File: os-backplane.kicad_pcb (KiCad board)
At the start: 4 copper layers, 195 x 95 mm, 160 parts, among them J10 FAN, J8 PWR, J9 FPANEL, Q1 AOD4189, Q10 MMBT3904, Q11 IRFML8244, Q2 AOD4189, Q3 BSS138, Q4 BSS138, Q5 CSD18504Q5A, Q6 CSD18504Q5A, Q7 CSD18503Q5A, Q8 MMBT3904, Q9 MMBT3906, U6 LM25116MHX, U7 LM25088-1MH

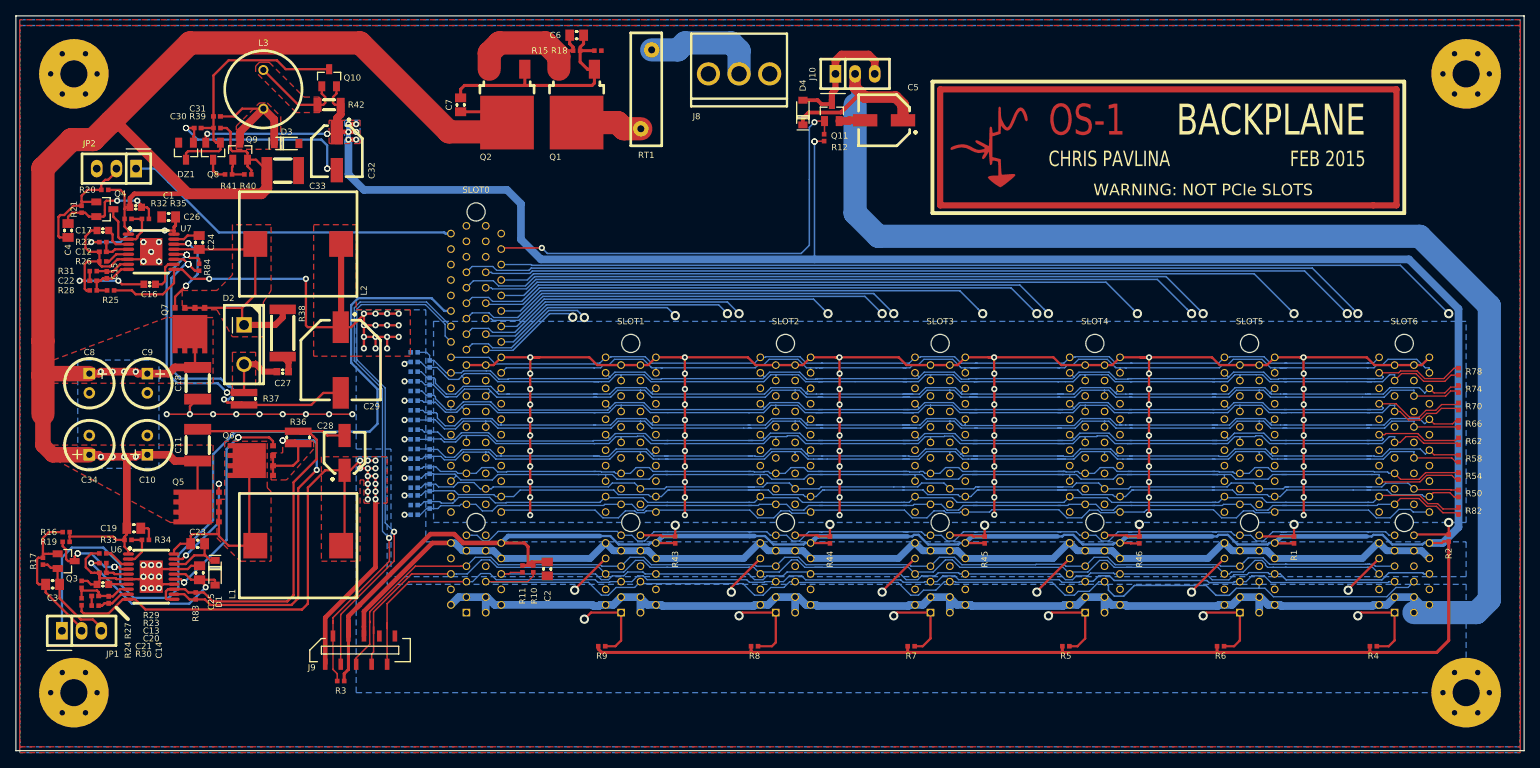
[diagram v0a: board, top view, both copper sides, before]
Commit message: Reannotated parts
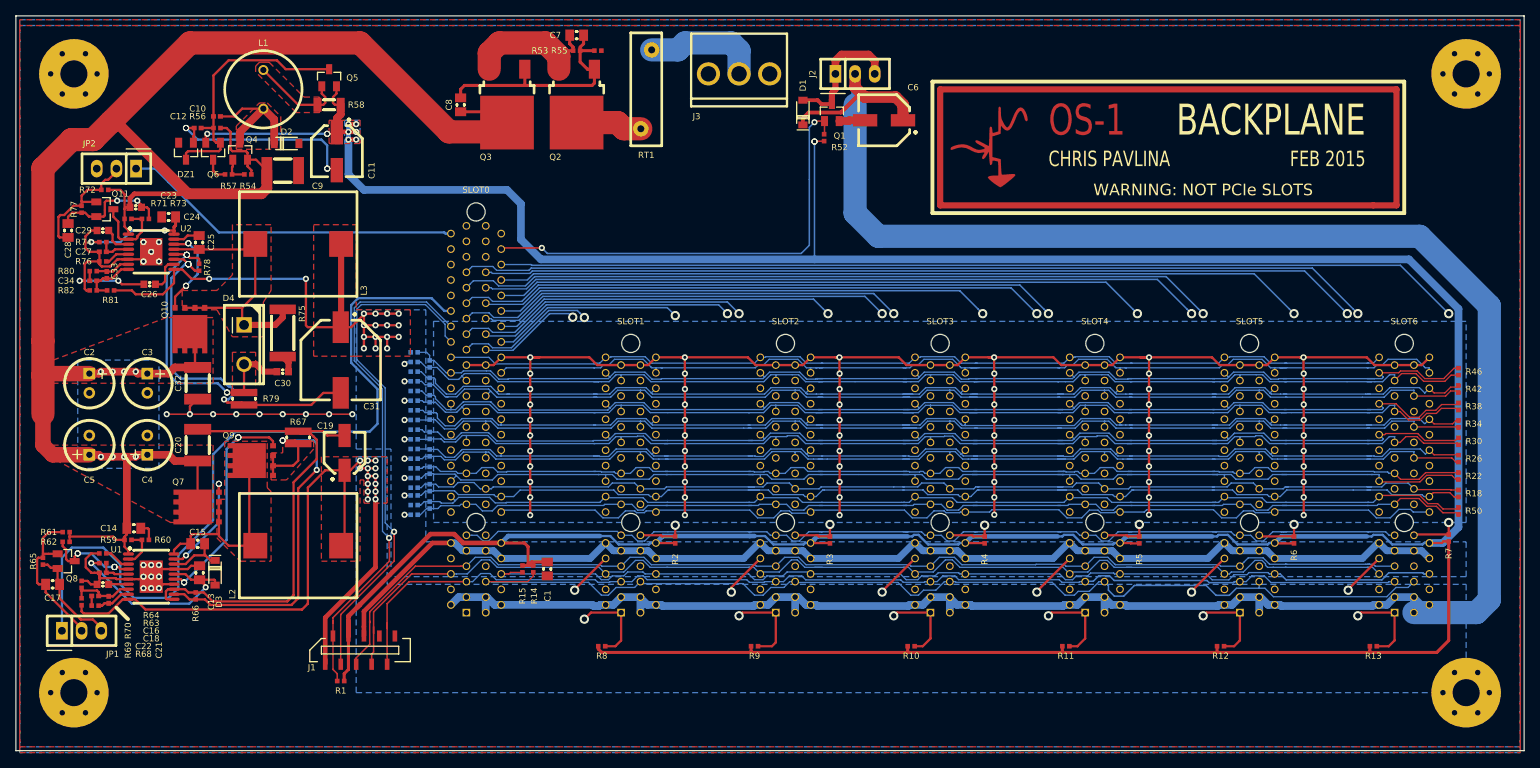
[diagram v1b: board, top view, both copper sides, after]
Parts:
- renumbered C2 to C1, C31 to C10, C32 to C11, C30 to C12, C25 to C13, C19 to C14, C23 to C15, C13 to C16, C3 to C17, C20 to C18, C28 to C19, C8 to C2, C11 to C20, C14 to C21, C21 to C22, C1 to C23, C26 to C24, C24 to C25, C16 to C26, C12 to C27, C4 to C28, C17 to C29, C9 to C3, C27 to C30, C29 to C31, C18 to C32, C15 to C33, C22 to C34, C10 to C4, C34 to C5, C5 to C6, C6 to C7, C7 to C8, C33 to C9, D4 to D1, D3 to D2, D1 to D3, D2 to D4, J9 to J1, J10 to J2, J8 to J3, L3 to L1, L1 to L2, L2 to L3, Q11 to Q1, Q7 to Q10, Q4 to Q11, Q1 to Q2, Q2 to Q3, Q9 to Q4, Q10 to Q5, Q8 to Q6, Q5 to Q7, Q3 to Q8, Q6 to Q9, R3 to R1, R7 to R10, R5 to R11, R6 to R12, R4 to R13, R10 to R14, R11 to R15, R47 to R16, R48 to R17, R50 to R18, R49 to R19, R43 to R2, R51 to R20, R52 to R21, R54 to R22, R53 to R23, R55 to R24, R56 to R25, R58 to R26, R57 to R27, R59 to R28, R60 to R29, R44 to R3, R62 to R30, R61 to R31, R63 to R32, R64 to R33, R66 to R34, R65 to R35, R67 to R36, R68 to R37, R70 to R38, R69 to R39, R45 to R4, R71 to R40, R72 to R41, R74 to R42, R73 to R43, R75 to R44, R76 to R45, R78 to R46, R77 to R47, R79 to R48, R80 to R49, R46 to R5, R82 to R50, R81 to R51, R12 to R52, R15 to R53, R40 to R54, R18 to R55, R39 to R56, R41 to R57, R42 to R58, R33 to R59, R1 to R6, R34 to R60, R16 to R61, R19 to R62, R23 to R63, R29 to R64, R17 to R65, R83 to R66, R36 to R67, R30 to R68, R24 to R69, R2 to R7, R27 to R70, R32 to R71, R20 to R72, R35 to R73, R22 to R74, R38 to R75, R26 to R76, R21 to R77, R84 to R78, R37 to R79, R9 to R8, R31 to R80, R25 to R81, R28 to R82, R8 to R9, U6 to U1, U7 to U2, W2 to W1, W1 to W2, W4 to W3, W3 to W4
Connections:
- R1 pad 2: Net-(R3-Pad2) -> +3.3SB
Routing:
- net +3.3SB: track 553.2 -> 554.1 mm
- net Net-(R3-Pad2): track 0.95 -> 0.00 mm
- added copper zone on F.Cu, net /Power/Supply3V3/CS+
- added copper zone on F.Cu, net /Power/Supply3V3/SW
- removed copper zone on F.Cu, net /Power/3CS
- removed copper zone on F.Cu, net /Power/3SW

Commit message: Added extra supports
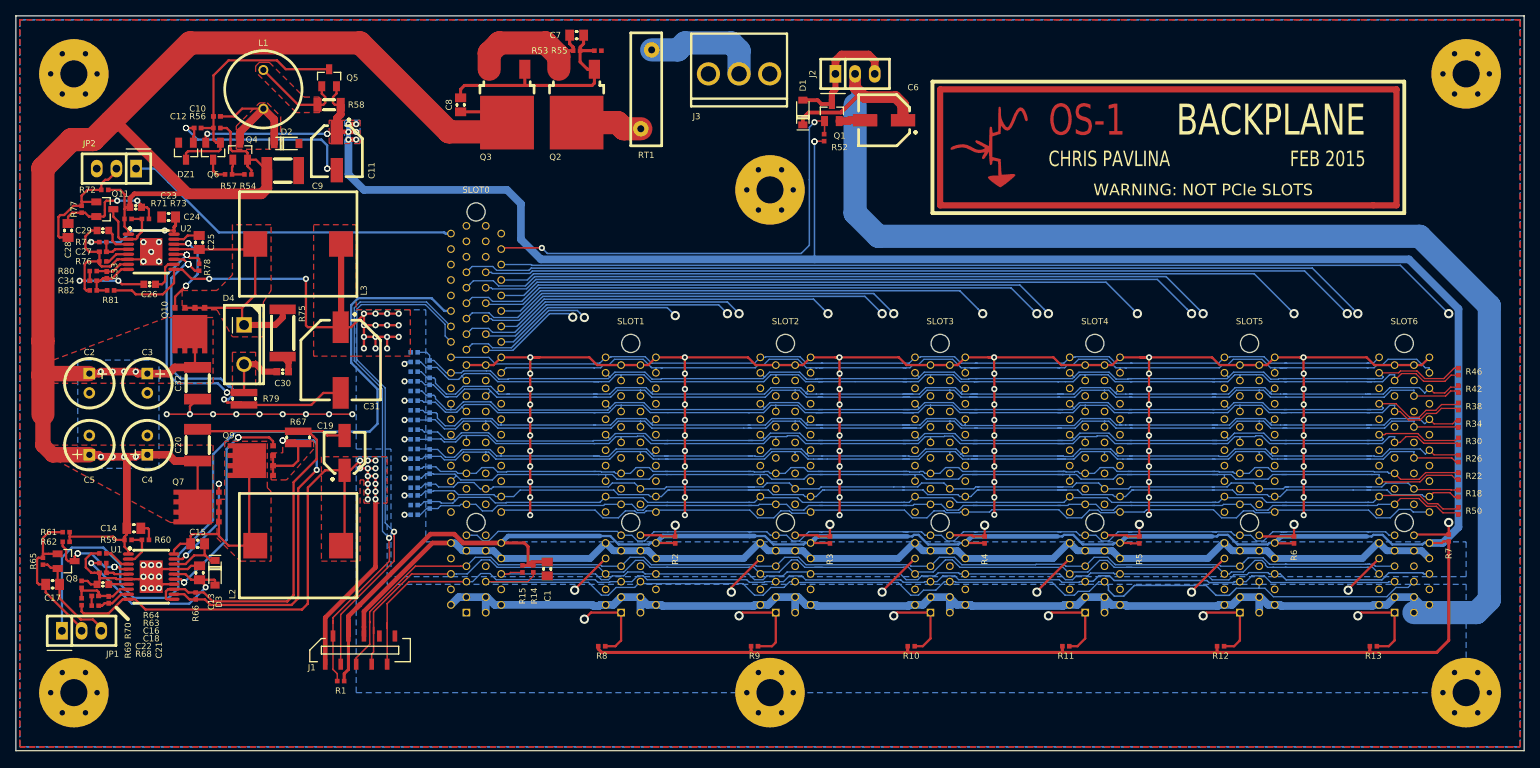
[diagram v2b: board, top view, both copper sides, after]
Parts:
- added MP5: SCREW, mech:SCREW-4-SUPPORTED, F.Cu at (125.0, 80.0)
- added MP6: SCREW, mech:SCREW-4-SUPPORTED, F.Cu at (125.0, 145.0)

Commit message: Added Easter egg
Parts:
- added G***: LOGO, LOGO, B.Cu at (215.0, 77.5)

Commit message: Silkscreen and 3D touchups
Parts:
- moved R72 4.00 mm to (35.0, 80.0), turned to 270 degrees
- moved R77 1.03 mm to (35.0, 82.2)
- turned JP2 to 0 degrees
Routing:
- net /Power/3V3EN: track 44.2 -> 51.6 mm
- net GND: track 422.6 -> 417.6 mm
- net /Power/Supply3V3/CS-: track 30.5 -> 27.4 mm
- net /Power/Supply3V3/CS+: track 39.8 -> 36.7 mm
- net Net-(C28-Pad1): track 17.3 -> 18.7 mm
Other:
- board text added: "- + -"
- board text added: "12V FAN"
- board text added: "16-25V 65W"
- board text added: "CPU"
- board text added: "DESPITE ITS DELICIOUS APPEARANCE, THE SOLDER IS NOT INTENDED FOR HUMAN CONSUMPTION."
- board text added: "DO NOT OBSTRUCT THE FLOW OF ELECTRONS OR POPULATE SLOTS WITH CHEESE."
- board text added: "JP1, JP2:"
- board text added: "OFF"
- board text added: "ON"
- board text added: "PANEL"
- board text added: "THIS OSCILLOSCOPE CONTAINS LARGE PARTS AND IS NOT SUITABLE FOR USE BY ADULTS OR GOLDFISH."

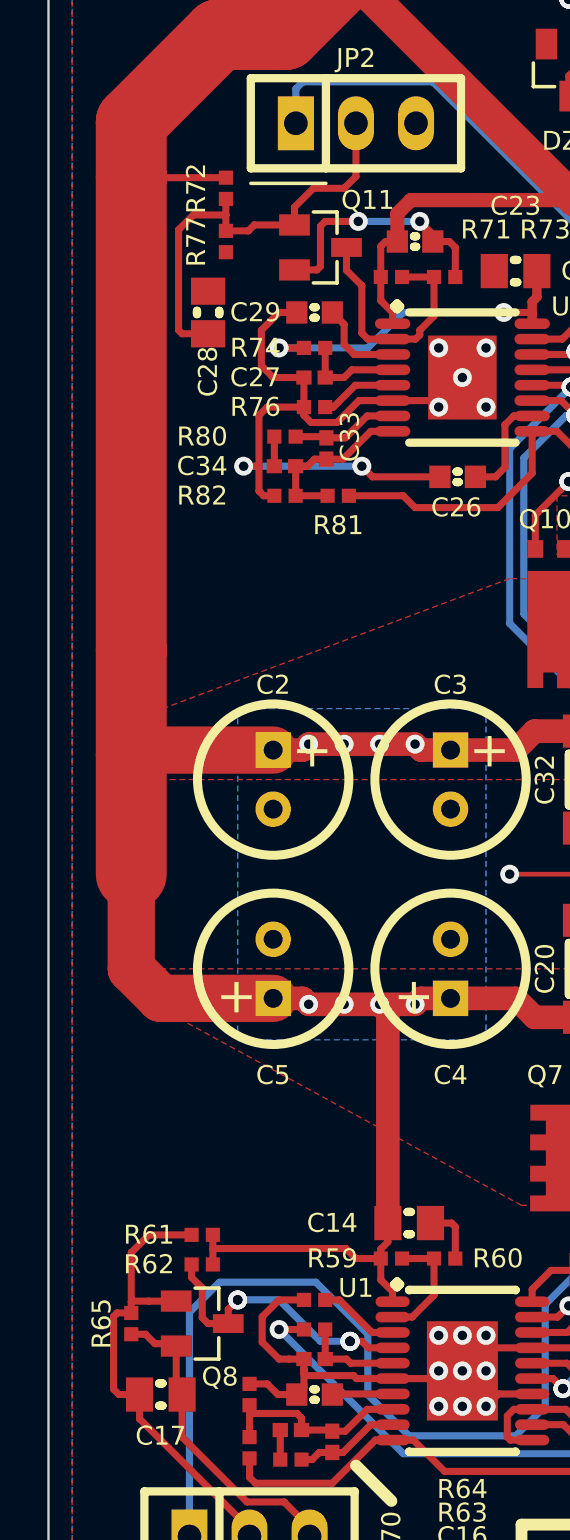
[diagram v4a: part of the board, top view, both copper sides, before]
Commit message: Changed BSS138 to MMUN221
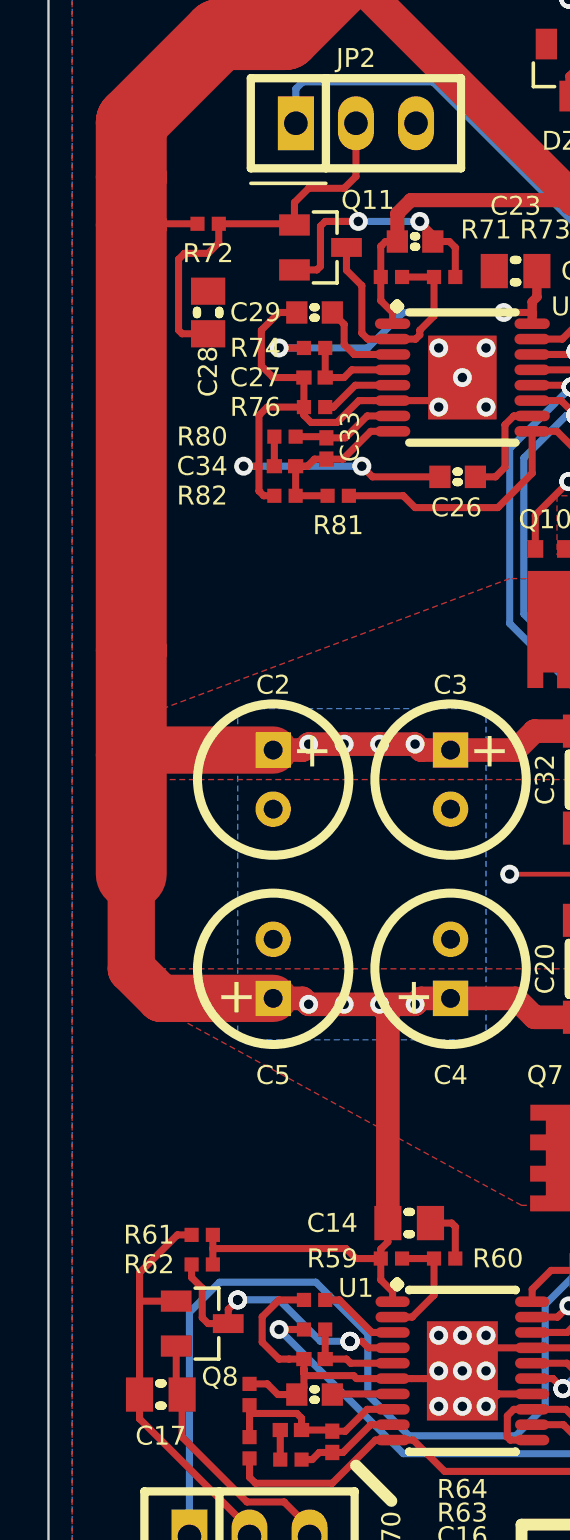
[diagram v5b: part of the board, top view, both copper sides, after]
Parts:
- removed R65, R77: 20k, IPC7351-Nominal:RESC1005X40
- Q11, Q8: value BSS138 -> MMUN2231L
- R61, R62, R72: value 130k -> 22k
- moved R72 1.68 mm to (34.2, 81.5), turned to 0 degrees
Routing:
- net Net-(C17-Pad1): track 20.3 -> 17.5 mm
- net GND: track 417.6 -> 415.6 mm
- net Net-(C28-Pad1): track 18.7 -> 17.0 mm
- net /Power/Supply12V/VIN: track 266.1 -> 264.9 mm

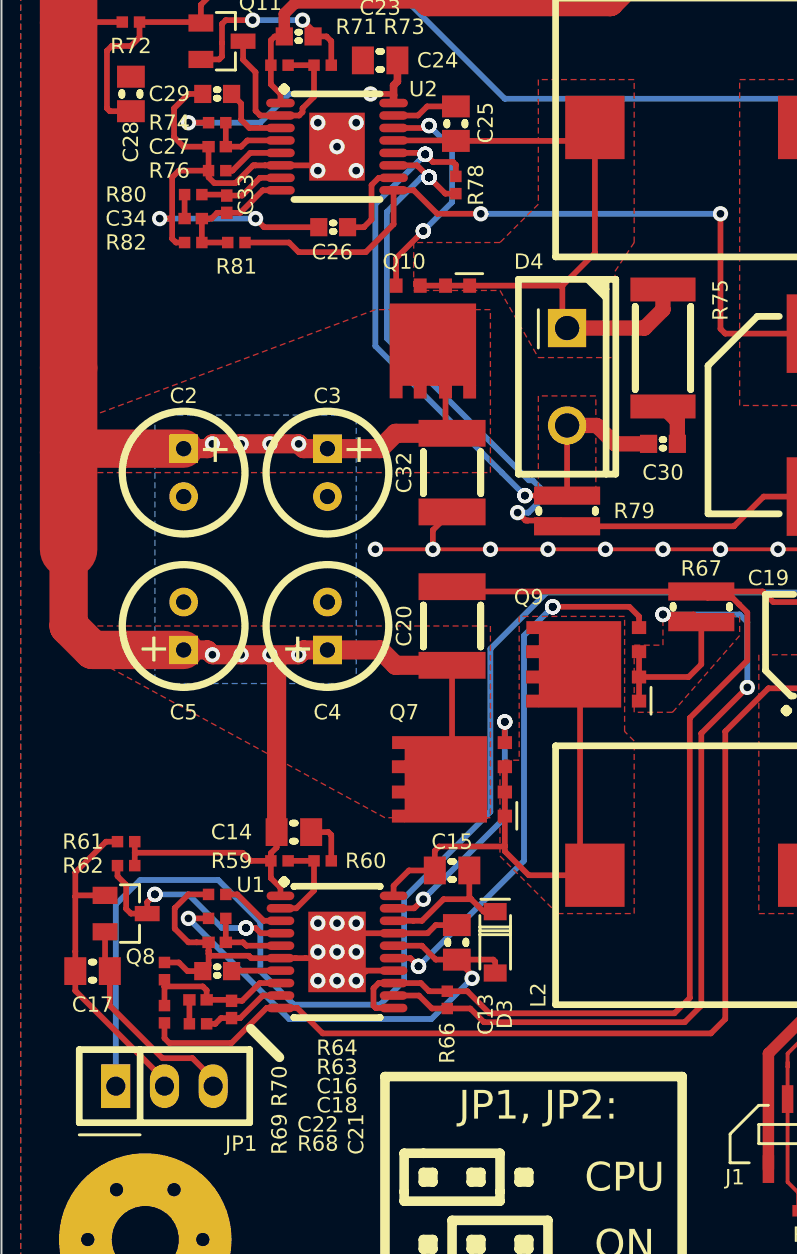
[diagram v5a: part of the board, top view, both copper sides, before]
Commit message: Added auto-renders
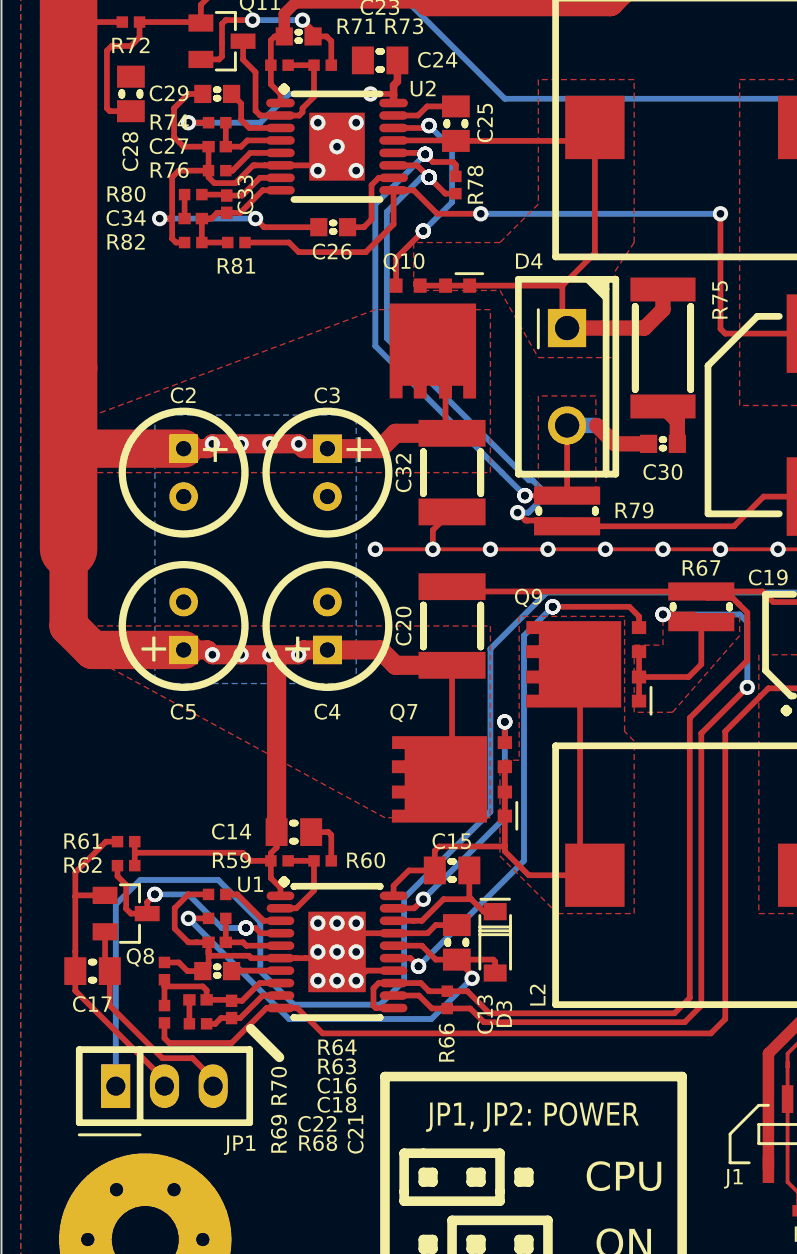
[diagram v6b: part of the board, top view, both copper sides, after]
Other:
- board text added: "JP1, JP2: POWER"
- board text removed: "JP1, JP2:"

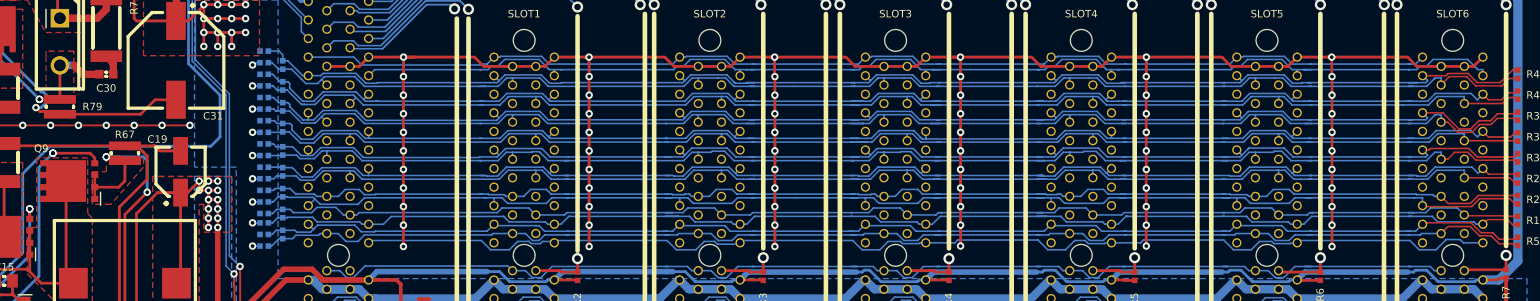
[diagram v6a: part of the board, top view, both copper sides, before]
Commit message: Corrected thermal reliefs
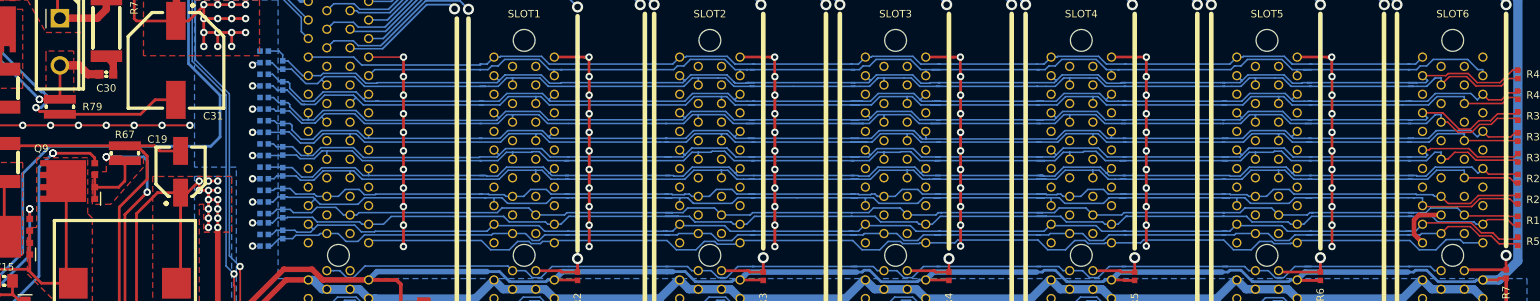
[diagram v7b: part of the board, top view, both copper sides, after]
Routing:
- net GND: track 415.6 -> 309.8 mm
- net /Power/Supply3V3/CS+: track 36.7 -> 38.3 mm
